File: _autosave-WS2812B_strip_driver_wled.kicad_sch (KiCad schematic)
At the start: 114 parts, among them J1 CH_1, J2 CH_2, J3 CH_3, J4 CH_4, J5 PWR_IN, J6 uPhone, J8 USB_C_Receptacle_USB2.0_16P, K1 RELAY_1, K2 RELAY_2, K3 RELAY_3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

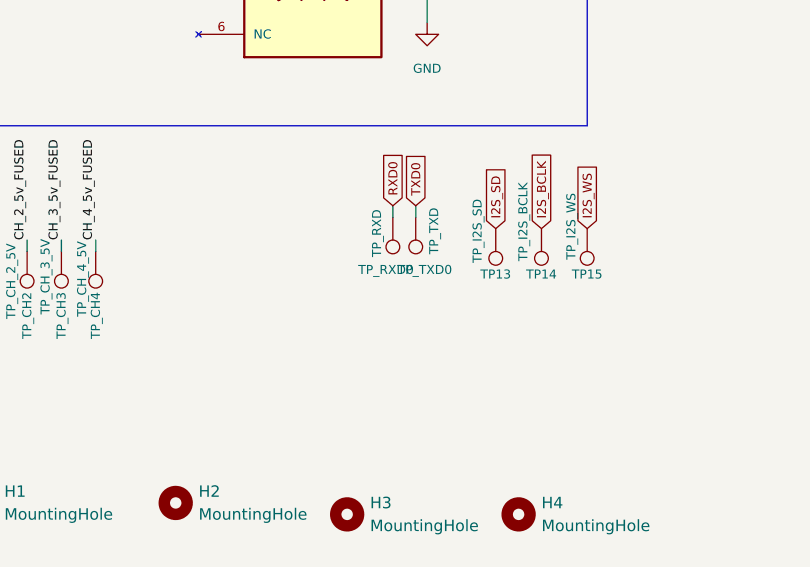
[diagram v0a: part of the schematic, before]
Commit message: reordered channels, renamed TP's, moved uC good led
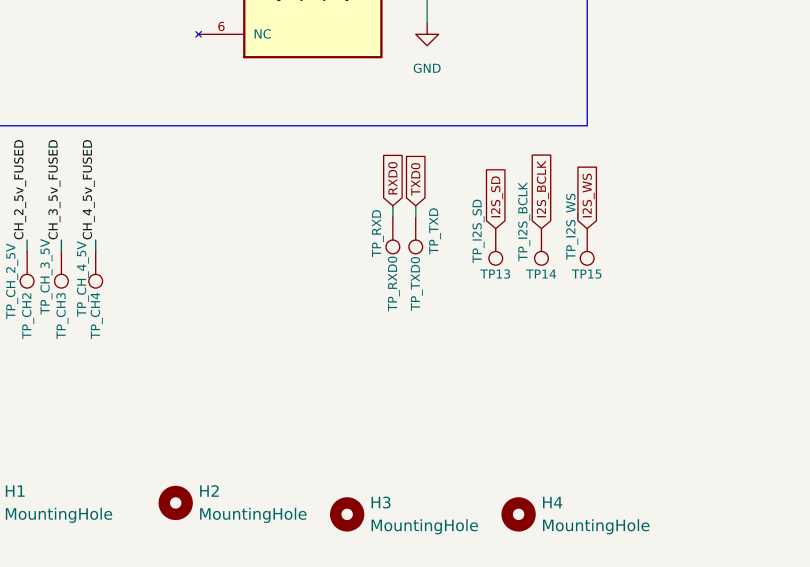
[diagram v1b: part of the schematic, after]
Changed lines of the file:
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@@
 		(dnp no)
 		(property "Reference" "TP_TXD0"
-			(at 265.176 179.832 0)
+			(at 264.16 181.356 90)
 			(effects
 				(font
@@
 		(dnp no)
 		(property "Reference" "TP_RXD0"
-			(at 260.858 179.832 0)
+			(at 261.62 181.356 90)
 			(effects
 				(font
